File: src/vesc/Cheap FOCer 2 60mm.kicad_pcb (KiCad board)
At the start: 6 copper layers, 80 x 100 mm, 158 parts, among them J1 Conn_01x02, J101 USB_C_Receptacle_USB2.0_16P, J2 Conn_01x03, J3 Conn_01x02, J7 Conn_02x03_Odd_Even, P4 HALL/Encoder, Q1 NCEP60T20, Q2 NCEP60T20, Q3 NCEP60T20, Q4 NCEP60T20, Q5 NCEP60T20, Q6 NCEP60T20, U1 HX4002, U2 DRV8301, U3 TCAN1462V, U3A1 TP2604-SR, U3B1 TP2604-SR, U3C1 TP2604-SR, U5 STM32F405RGT6, X1 24MHz

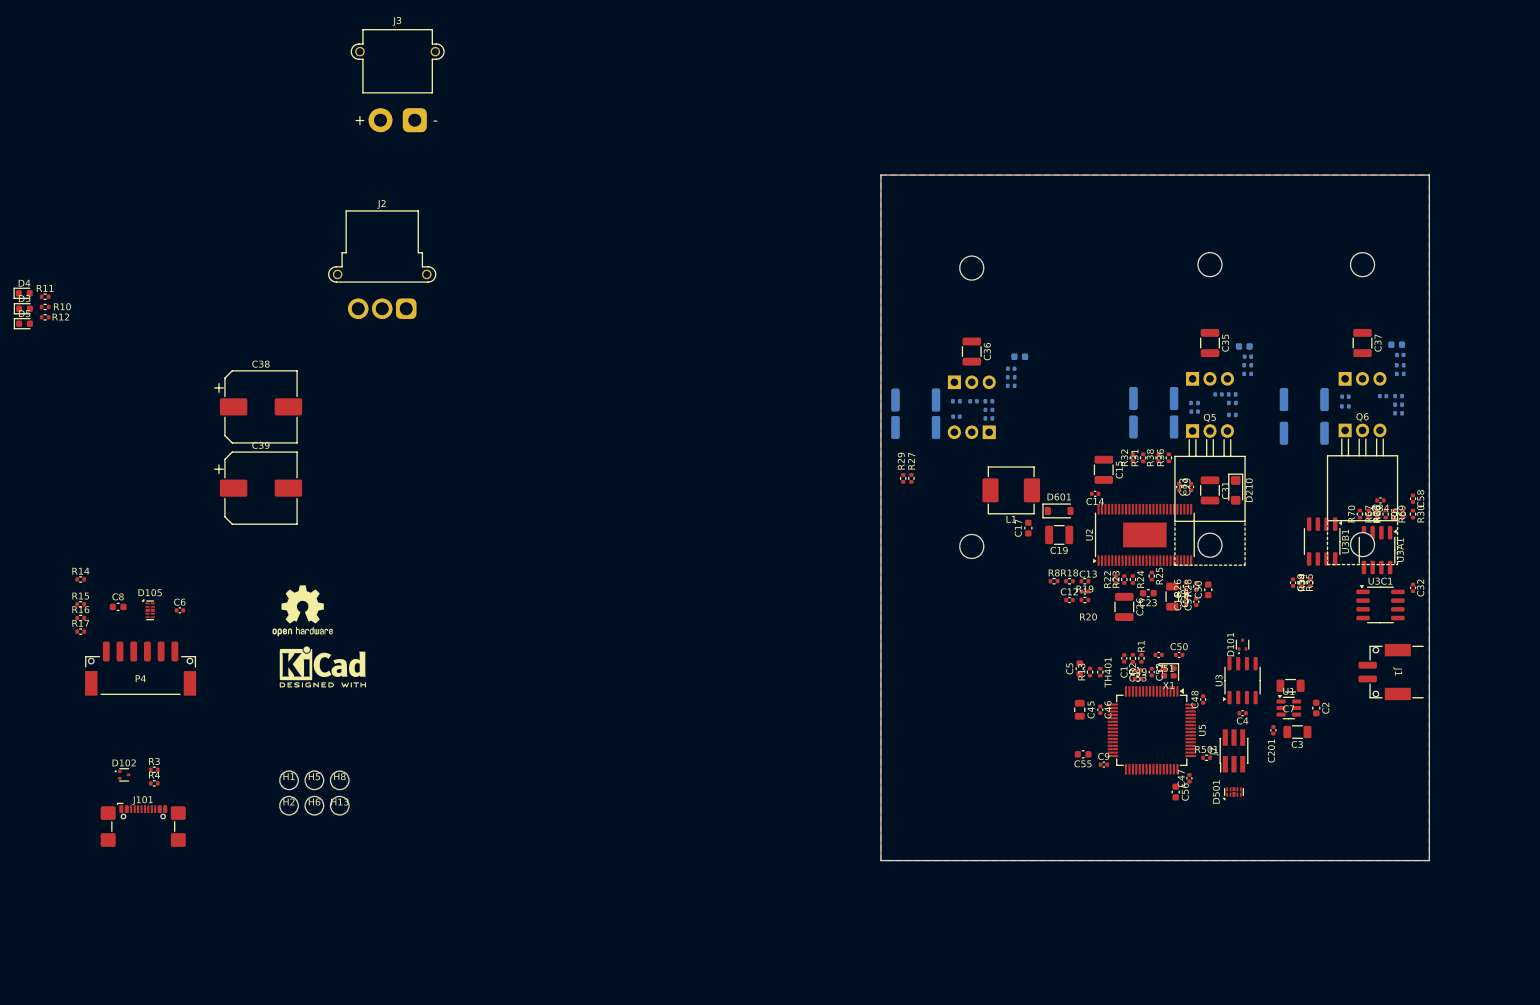
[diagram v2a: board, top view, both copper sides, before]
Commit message: MOSFET routing almost
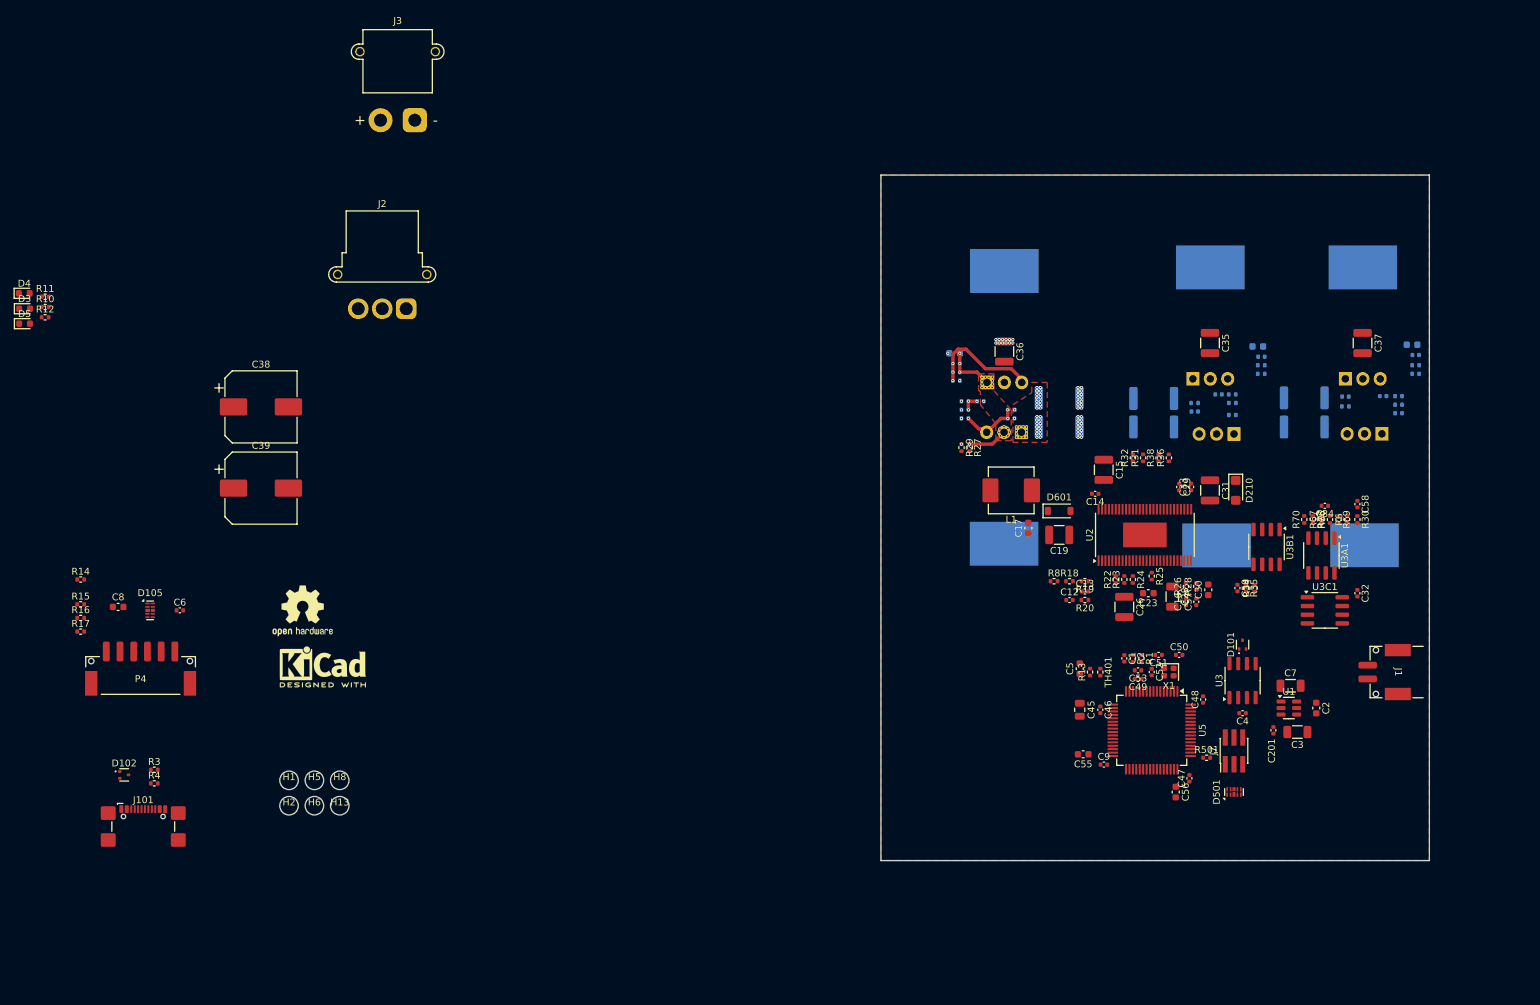
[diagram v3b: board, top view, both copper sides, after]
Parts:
- Q1, Q2, Q3, Q4: footprint Package_TO_SOT_THT:TO-220-3_Horizontal_TabUp -> Bluesat:TO-220-3-heatsink-pad-tabdown
- Q5, Q6: footprint Package_TO_SOT_THT:TO-220-3_Horizontal_TabUp -> Bluesat:TO-220-3-heatsink-pad-tabdown; moved to B.Cu
- moved R57 20.9 mm to (126.0, 82.5), turned to 180 degrees
- moved R56 20.9 mm to (126.0, 86.8), turned to 180 degrees
- moved Q5 16.9 mm to (154.1, 101.9), turned to 180 degrees
- moved Q6 16.6 mm to (175.7, 101.9), turned to 180 degrees
- moved Q4 15.9 mm to (123.1, 101.7)
- moved Q2 14.4 mm to (142.9, 65.6)
- moved Q3 14.4 mm to (165.2, 65.6)
- moved Q1 14.3 mm to (112.9, 66.1)
- moved R27 9.61 mm to (112.9, 89.8)
- moved R29 9.61 mm to (111.8, 89.8)
- moved C18 9.51 mm to (110.8, 76.0), turned to 0 degrees
- moved C32 8.15 mm to (169.5, 111.0)
- moved C34 8.15 mm to (164.8, 98.2)
- moved C58 8.15 mm to (169.5, 98.0)
- moved C59 8.15 mm to (152.0, 110.2)
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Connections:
- net SPA renamed GND
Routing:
- net Net-(Q1-G): track 0.00 -> 15.6 mm, vias 0 -> 3
- net /Mosfet driver/H1_VS: track 0.00 -> 11.3 mm, vias 0 -> 25
- net Net-(Q4-G): track 0.00 -> 7.00 mm, vias 0 -> 3
- net Net-(C40-Pad2): track 0.00 -> 2.50 mm, vias 0 -> 3
- net SNA: vias 0 -> 42
- net Net-(U2-BST_A): vias 0 -> 1
- net GND: vias 0 -> 43
- net /Mosfet driver/GL_A: vias 0 -> 1
- net /Mosfet driver/GH_A: vias 0 -> 1
- added copper zone on F.Cu, net /Mosfet driver/H1_VS
- added copper zone on F.Cu, net SNA

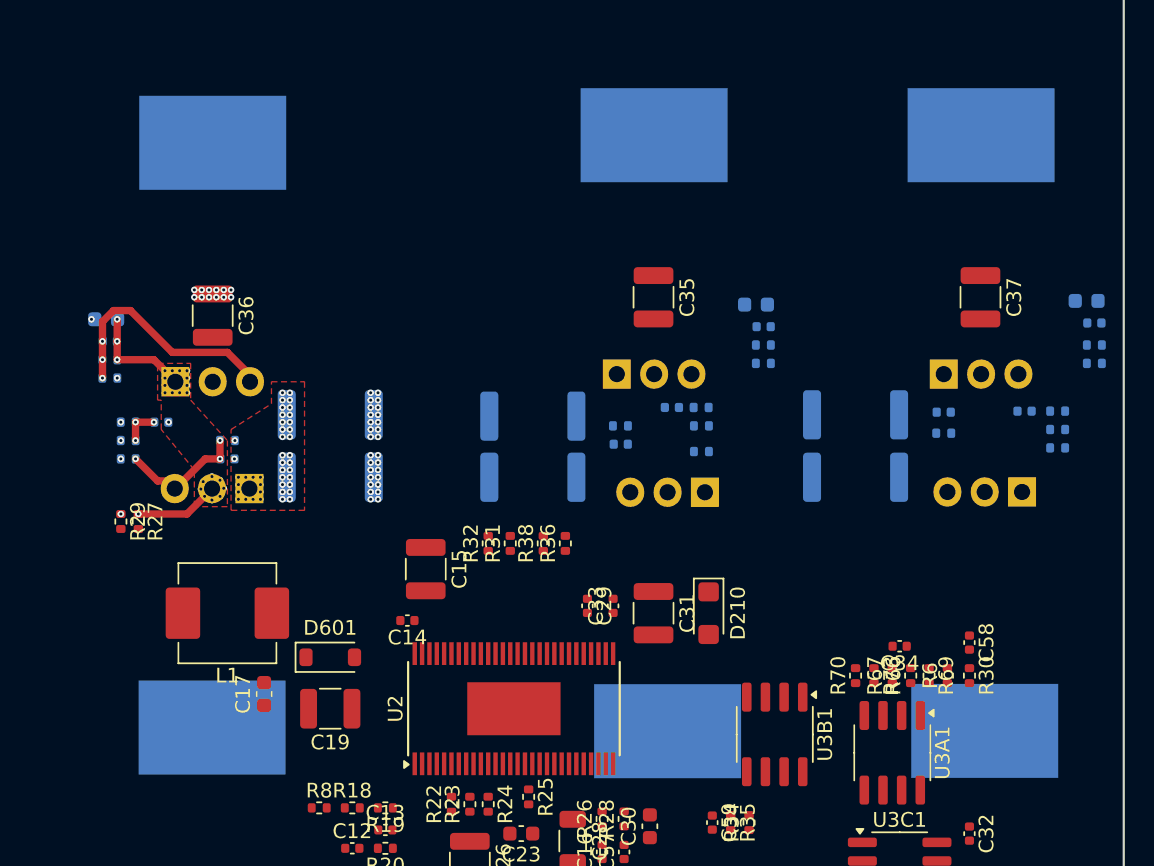
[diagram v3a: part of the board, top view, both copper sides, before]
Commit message: mosfet routing
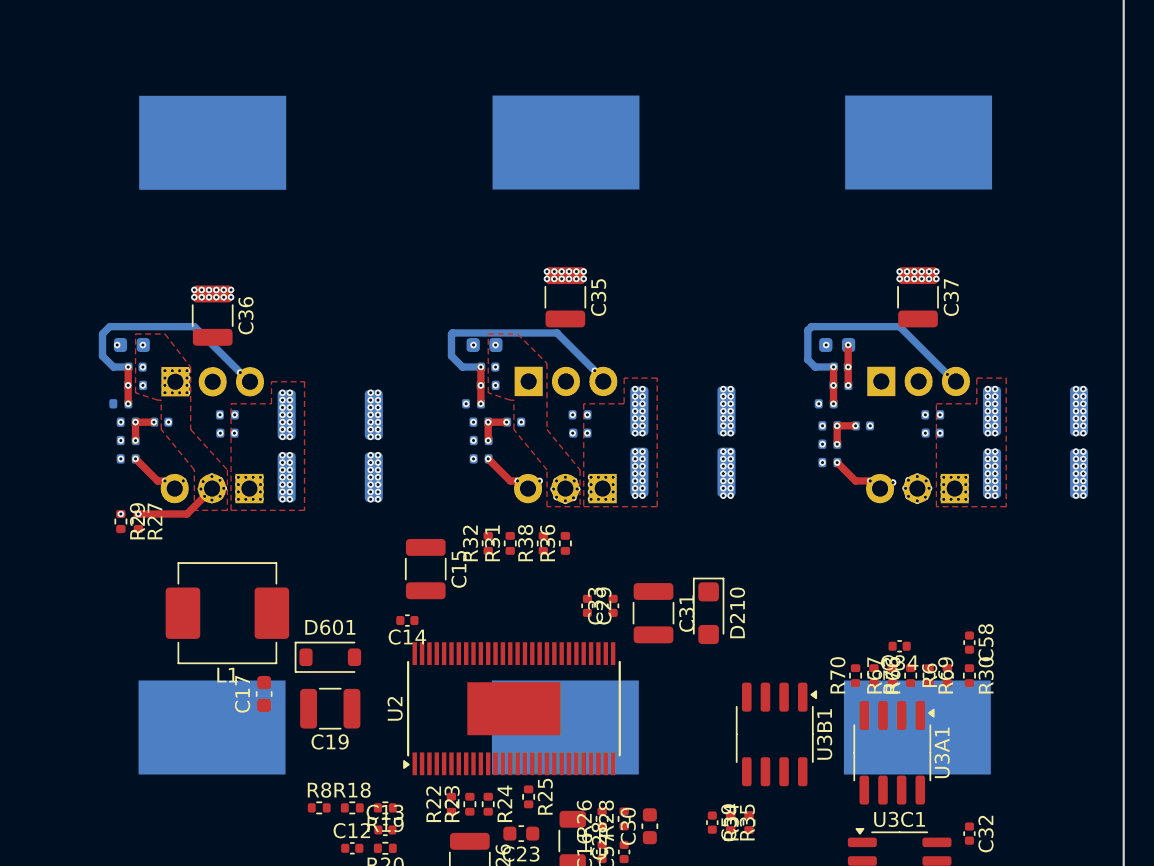
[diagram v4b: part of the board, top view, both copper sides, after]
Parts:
- moved R42 19.9 mm to (135.8, 81.8), turned to 180 degrees
- moved C63 18.9 mm to (136.8, 79.2)
- moved R45 18.9 mm to (136.8, 80.5)
- moved C24 18.7 mm to (136.5, 77.8)
- moved R43 18.5 mm to (159.8, 81.8), turned to 180 degrees
- moved C66 17.5 mm to (160.8, 79.2)
- moved R46 17.5 mm to (160.8, 80.5)
- moved C27 17.2 mm to (160.5, 77.8)
- moved R39 15.5 mm to (160.0, 83.2)
- moved R49 15.5 mm to (160.0, 85.8), turned to 180 degrees
- moved R55 15.5 mm to (160.0, 84.5), turned to 0 degrees
- moved R54 15.0 mm to (136.2, 83.0), turned to 0 degrees
- moved R37 15.0 mm to (136.3, 84.2), turned to 0 degrees
- moved R48 15.0 mm to (136.3, 85.5), turned to 180 degrees
- moved R60 12.3 mm to (174.0, 82.2), turned to 180 degrees
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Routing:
- net Net-(Q3-G): track 0.00 -> 17.4 mm, vias 0 -> 4
- net Net-(Q2-G): track 0.00 -> 17.2 mm, vias 0 -> 4
- net Net-(Q6-G): track 0.00 -> 8.49 mm, vias 0 -> 5
- net Net-(Q5-G): track 0.00 -> 8.05 mm, vias 0 -> 5
- net /Mosfet driver/H1_VS: track 11.3 -> 5.01 mm
- net /Mosfet driver/H3_VS: track 0.00 -> 2.75 mm, vias 0 -> 12
- net Net-(C42-Pad2): track 0.00 -> 2.50 mm, vias 0 -> 3
- net Net-(C41-Pad2): track 0.00 -> 2.50 mm, vias 0 -> 3
- net Net-(Q1-G): track 15.6 -> 17.1 mm, vias 3 -> 4
- net Net-(Q4-G): track 7.00 -> 8.17 mm, vias 3 -> 5
- net SNC: vias 0 -> 42
- net SNB: vias 0 -> 42
- net Net-(U2-BST_C): vias 0 -> 1
- net Net-(U2-BST_B): vias 0 -> 1
- net GND: vias 43 -> 127
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- added copper zone on F.Cu, net /Mosfet driver/H2_VS
- added copper zone on F.Cu, net SNB
- added copper zone on F.Cu, net SNC

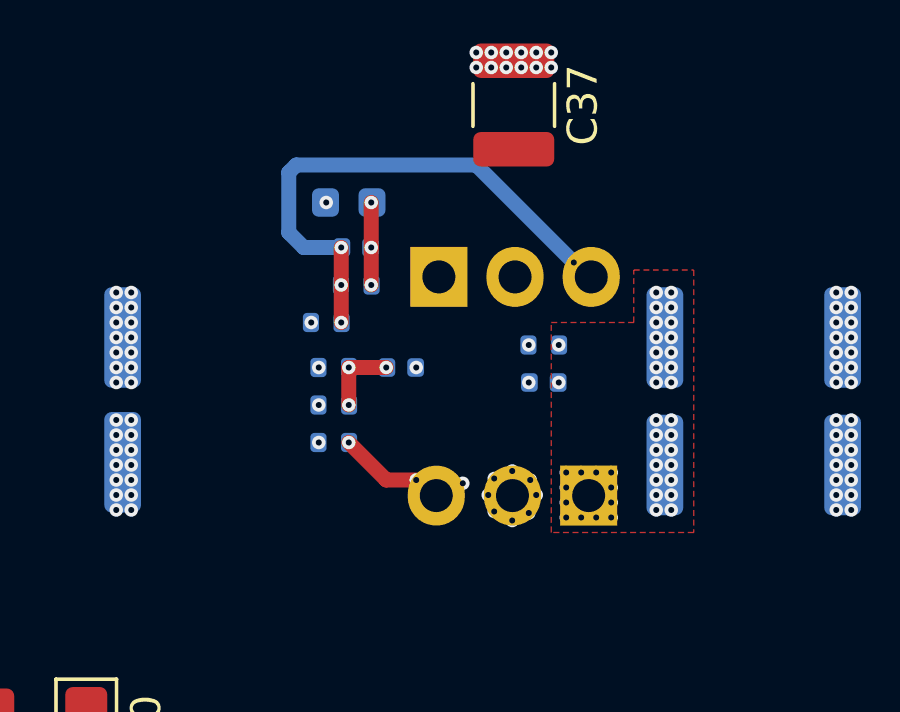
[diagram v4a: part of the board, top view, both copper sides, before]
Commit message: MOSFET filled zones
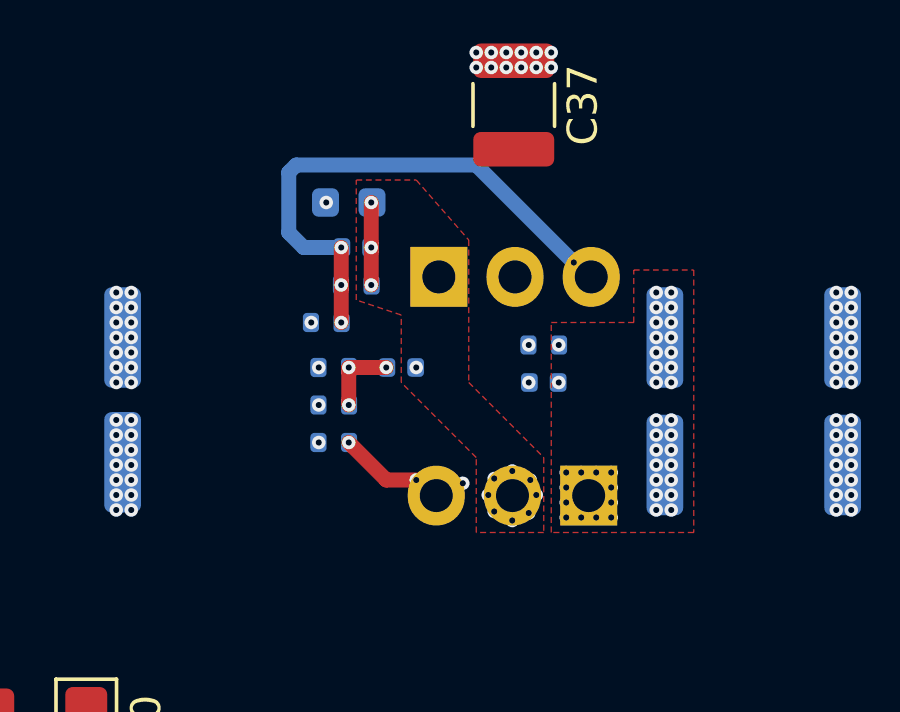
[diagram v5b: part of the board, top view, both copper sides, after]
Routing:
- added copper zone on F.Cu, net /Mosfet driver/H3_VS
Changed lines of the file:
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@@
+	)
+	(zone
+		(net 23)
+		(net_name "/Mosfet driver/H3_VS")
+		(layer "F.Cu")
+		(hatch edge 0.5)
+		(priority 8)
+		(connect_pads yes
+			(clearance 0.4)
+		)
+		(min_thickness 0.25)
+		(filled_areas_thickness no)
+		(fill yes
+			(thermal_gap 0.5)
+			(thermal_bridge_width 0.5)
+		)
+		(polygon
+			(pts
+				(xy 167 88.75) (xy 164.75 88.75) (xy 164.75 86.25) (xy 162.25 83.75) (xy 162.25 81.5) (xy 160.75 81)
+				(xy 160.75 77) (xy 162.75 77) (xy 164.5 79) (xy 164.5 83.75) (xy 167 86.25)
+			)
+		)
 	)
 	(zone

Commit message: more MOSFET zones
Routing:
- added copper zone on In3.Cu, net SNA
- added copper zone on In3.Cu, net SNB
- added copper zone on In3.Cu, net SNC
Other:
- board size 80 x 100 mm -> 72.8 x 100 mm
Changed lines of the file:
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@@
 	)
 	(gr_rect
-		(start 100 50)
+		(start 107.25 50)
 		(end 180 150)
 		(stroke
@@
 		(polygon
 			(pts
-				(xy 180 50) (xy 180 150) (xy 100 150) (xy 100 50)
+				(xy 180 50) (xy 180 150) (xy 107.25 150) (xy 107.25 50)
 			)
 		)
@@
 			)
 		)
+	)
+	(zone
+		(net 28)
+		(net_name "SNB")
+		(layer "In3.Cu")
+		(hatch edge 0.5)
+		(priority 10)
+		(connect_pads yes
+			(clearance 0.4)
+		)
+		(min_thickness 0.25)
+		(filled_areas_thickness no)
+		(fill yes
+			(thermal_gap 0.5)
+			(thermal_bridge_width 0.5)
+		)
+		(polygon
+			(pts
+				(xy 148.25 88.75) (xy 143.25 88.75) (xy 143.25 81.75) (xy 146 81.75) (xy 146 80) (xy 148.25 80)
+			)
+		)
+	)
+	(zone
+		(net 29)
+		(net_name "SNC")
+		(layer "In3.Cu")
+		(hatch edge 0.5)
+		(priority 9)
+		(connect_pads yes
+			(clearance 0.4)
+		)
+		(min_thickness 0.25)
+		(filled_areas_thickness no)
+		(fill yes
+			(thermal_gap 0.5)
+			(thermal_bridge_width 0.5)
+		)
+		(polygon
+			(pts
+				(xy 167.25 88.75) (xy 172 88.75) (xy 172 80) (xy 170 80) (xy 170 81.75) (xy 167.25 81.75)
+			)
+		)
+	)
+	(zone
+		(net 26)
+		(net_name "SNA")
+		(layer "In3.Cu")
+		(hatch edge 0.5)
+		(priority 11)
+		(connect_pads yes
+			(clearance 0.4)
+		)
+		(min_thickness 0.25)
+		(filled_areas_thickness no)
+		(fill yes
+			(thermal_gap 0.5)
+			(thermal_bridge_width 0.5)
+		)
+		(polygon
+			(pts
+				(xy 124.25 89) (xy 119.25 89) (xy 119.25 81.75) (xy 122 81.75) (xy 122 80.25) (xy 124.25 80.25)
+			)
+		)
